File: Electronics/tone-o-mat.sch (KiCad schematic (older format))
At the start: 68 parts

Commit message: First iteration of PCB.
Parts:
- removed C?: 100uF, symbol Device:C
- removed D?: 1N4148, Diode_THT:D_DO-35_SOD27_P7.62mm_Horizontal, symbol Diode:1N4148
- removed LS?: Speaker, symbol Device:Speaker
- removed Q? (x2): BC337, Package_TO_SOT_THT:TO-92_Inline, symbol Transistor_BJT:BC337
- removed RV?: 1k, symbol Device:R_POT
- removed RV?: 4k7, symbol Device:R_POT
- removed SW?: POWER, symbol Switch:SW_DIP_x01
- removed SW?: VIBRATO, symbol Switch:SW_DIP_x01
- added C1, C3, C5, C7: 0.1uF, Capacitor_SMD:C_1206_3216Metric_Pad1.33x1.80mm_HandSolder, symbol Device:C
- added C10: 2.2uF, Capacitor_SMD:C_1206_3216Metric_Pad1.33x1.80mm_HandSolder, symbol Device:C
- added C12: 27nF, Capacitor_SMD:C_1206_3216Metric_Pad1.33x1.80mm_HandSolder, symbol Device:C
- added C9: 100uF, Capacitor_THT:CP_Radial_D5.0mm_P2.00mm, symbol Device:C
- added D1: 1N4148, Diode_THT:D_DO-35_SOD27_P7.62mm_Horizontal, symbol Diode:1N4148
- added H1, H2, H3: MountingHole_Pad, MountingHole:MountingHole_3.2mm_M3_DIN965_Pad, symbol Mechanical:MountingHole_Pad
- added J21: USB_C_Receptacle_USB2.0, Connector_USB:USB_C_Receptacle_Amphenol_12401548E4-2A, symbol Connector:USB_C_Receptacle_USB2.0
- added LS1: Speaker, Connector_PinHeader_2.54mm:PinHeader_1x02_P2.54mm_Vertical, symbol Device:Speaker
- added Q1, Q3: BC337, Package_TO_SOT_THT:TO-92_Inline, symbol Transistor_BJT:BC337
- added R10: 2.45k, Resistor_THT:R_Axial_DIN0309_L9.0mm_D3.2mm_P12.70mm_Horizontal, symbol Device:R
- added R12: 2.59k, Resistor_THT:R_Axial_DIN0309_L9.0mm_D3.2mm_P12.70mm_Horizontal, symbol Device:R
- added R14: 2.75k, Resistor_THT:R_Axial_DIN0309_L9.0mm_D3.2mm_P12.70mm_Horizontal, symbol Device:R
- added R16: 2.91k, Resistor_THT:R_Axial_DIN0309_L9.0mm_D3.2mm_P12.70mm_Horizontal, symbol Device:R
- added R18: 3.08k, Resistor_THT:R_Axial_DIN0309_L9.0mm_D3.2mm_P12.70mm_Horizontal, symbol Device:R
- added R2: 33.3k, Resistor_THT:R_Axial_DIN0309_L9.0mm_D3.2mm_P12.70mm_Horizontal, symbol Device:R
- added R20: 3.27k, Resistor_THT:R_Axial_DIN0309_L9.0mm_D3.2mm_P12.70mm_Horizontal, symbol Device:R
- added R22: 3.46k, Resistor_THT:R_Axial_DIN0309_L9.0mm_D3.2mm_P12.70mm_Horizontal, symbol Device:R
- added R24: 3.66k, Resistor_THT:R_Axial_DIN0309_L9.0mm_D3.2mm_P12.70mm_Horizontal, symbol Device:R
- added R26: 3.88k, Resistor_THT:R_Axial_DIN0309_L9.0mm_D3.2mm_P12.70mm_Horizontal, symbol Device:R
- added R28: 4.11k, Resistor_THT:R_Axial_DIN0309_L9.0mm_D3.2mm_P12.70mm_Horizontal, symbol Device:R
- added R30: 4.35k, Resistor_THT:R_Axial_DIN0309_L9.0mm_D3.2mm_P12.70mm_Horizontal, symbol Device:R
- added R32: 4.59k, Resistor_THT:R_Axial_DIN0309_L9.0mm_D3.2mm_P12.70mm_Horizontal, symbol Device:R
- added R34: 4.84k, Resistor_THT:R_Axial_DIN0309_L9.0mm_D3.2mm_P12.70mm_Horizontal, symbol Device:R
- added R36: 5.15k, Resistor_THT:R_Axial_DIN0309_L9.0mm_D3.2mm_P12.70mm_Horizontal, symbol Device:R
- added R38: 5.49k, Resistor_THT:R_Axial_DIN0309_L9.0mm_D3.2mm_P12.70mm_Horizontal, symbol Device:R
- added R4: 2.05k, Resistor_THT:R_Axial_DIN0309_L9.0mm_D3.2mm_P12.70mm_Horizontal, symbol Device:R
- added R40: 5.85k, Resistor_THT:R_Axial_DIN0309_L9.0mm_D3.2mm_P12.70mm_Horizontal, symbol Device:R
- added R41, R57, R59: 68k, Resistor_SMD:R_1206_3216Metric_Pad1.30x1.75mm_HandSolder, symbol Device:R
- added R43, R53: 4k7, Resistor_SMD:R_1206_3216Metric_Pad1.30x1.75mm_HandSolder, symbol Device:R
- added R45: 270k, Resistor_SMD:R_1206_3216Metric_Pad1.30x1.75mm_HandSolder, symbol Device:R
- added R47: 1k, Resistor_SMD:R_1206_3216Metric_Pad1.30x1.75mm_HandSolder, symbol Device:R
- added R49: 680R, Resistor_SMD:R_1206_3216Metric_Pad1.30x1.75mm_HandSolder, symbol Device:R
- added R51: 10M, Resistor_SMD:R_1206_3216Metric_Pad1.30x1.75mm_HandSolder, symbol Device:R
- added R55: 56R, Resistor_SMD:R_1206_3216Metric_Pad1.30x1.75mm_HandSolder, symbol Device:R
- added R6: 2.18k, Resistor_THT:R_Axial_DIN0309_L9.0mm_D3.2mm_P12.70mm_Horizontal, symbol Device:R
- added R61: 3k3, Resistor_SMD:R_1206_3216Metric_Pad1.30x1.75mm_HandSolder, symbol Device:R
- added R8: 2.32k, Resistor_THT:R_Axial_DIN0309_L9.0mm_D3.2mm_P12.70mm_Horizontal, symbol Device:R
- added RV1: 4k7, Potentiometer_THT:Potentiometer_Alps_RK09K_Single_Vertical, symbol Device:R_POT
- added RV2: 1k, Potentiometer_THT:Potentiometer_Alps_RK097_Single_Horizontal, symbol Device:R_POT
- added SW1: VIBRATO, Button_Switch_THT:OS102011MS2QN1, symbol Switch:SW_DIP_x01
- added SW2: POWER, Button_Switch_THT:OS102011MS2QN1, symbol Switch:SW_DIP_x01
- added U2: NE555PS, Package_SO:SOIC-8_3.9x4.9mm_P1.27mm, symbol Timer:NE555PS
- C11, C13, C2, C4, C6, C8: renamed from C?; footprint (none) -> Capacitor_THT:C_Disc_D3.0mm_W2.0mm_P2.50mm
- J1, J16, J4, J9: renamed from J?; footprint (none) -> Connector_Pin:Tone-O-Mat-Left-Pad
- J10, J12, J14, J17, J19, J2, J5, J7: renamed from J?; footprint (none) -> Connector_Pin:Tone-O-Mat-Top-Pad
- J11, J13, J18, J6: renamed from J?; footprint (none) -> Connector_Pin:Tone-O-Mat-Mid-Pad
- J15, J20, J3, J8: renamed from J?; footprint (none) -> Connector_Pin:Tone-O-Mat-Right-Pad
- R1, R11, R13, R15, R17, R19, R21, R23, R25, R27, R29, R3, R31, R33, R35, R37, R39, R5, R7, R9: renamed from R?; footprint (none) -> Resistor_SMD:R_1206_3216Metric_Pad1.30x1.75mm_HandSolder
- R42, R44, R46, R48, R50, R52, R54, R56, R58, R60, R62: renamed from R?; footprint (none) -> Resistor_THT:R_Axial_DIN0309_L9.0mm_D3.2mm_P12.70mm_Horizontal
- STYLUS1: renamed from STYLUS; footprint (none) -> Connector_Pin:Pin_D1.3mm_L11.0mm
- U1: renamed from U?; footprint (none) -> Package_DIP:DIP-8_W7.62mm_LongPads
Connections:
- net +5V: now also C9.1, J21.A4 (VBUS), J21.A9 (VBUS), J21.B4 (VBUS), J21.B9 (VBUS), Q1.1 (C), R41.2, R43.1, R47.1, U2.4 (R), U2.8 (VCC)
- net GND: now also J21.A1 (GND), J21.A12 (GND), J21.B1 (GND), J21.B12 (GND), SW2.1
- net at J1.1 (Pin_1), R1.1, R3.2: now also R2.1, R4.2
- net at R1.2, R50.1: now also R2.2, R49.1
- net at J2.1 (Pin_1), R3.1, R5.2: now also R4.1, R6.2
- net at J3.1 (Pin_1), R5.1, R7.2: now also R6.1, R8.2
- net at J4.1 (Pin_1), R7.1, R9.2: now also R10.2, R8.1
- net at J5.1 (Pin_1), R11.2, R9.1: now also R10.1, R12.2
- net at J6.1 (Pin_1), R11.1, R13.2: now also R12.1, R14.2
- net at J7.1 (Pin_1), R13.1, R15.2: now also R14.1, R16.2
- net at J8.1 (Pin_1), R15.1, R17.2: now also R16.1, R18.2
- net at J9.1 (Pin_1), R17.1, R19.2: now also R18.1, R20.2
- net at J10.1 (Pin_1), R19.1, R21.2: now also R20.1, R22.2
- net at J11.1 (Pin_1), R21.1, R23.2: now also R22.1, R24.2
- net at J12.1 (Pin_1), R23.1, R25.2: now also R24.1, R26.2
- net at J13.1 (Pin_1), R25.1, R27.2: now also R26.1, R28.2
- net at J14.1 (Pin_1), R27.1, R29.2: now also R28.1, R30.2
- net at J15.1 (Pin_1), R29.1, R31.2: now also R30.1, R32.2
- net at J16.1 (Pin_1), R31.1, R33.2: now also R32.1, R34.2
- net at J17.1 (Pin_1), R33.1, R35.2: now also R34.1, R36.2
- net at J18.1 (Pin_1), R35.1, R37.2: now also R36.1, R38.2
- net at J19.1 (Pin_1), R37.1, R39.2: now also R38.1, R40.2
- net at J20.1 (Pin_1), R39.1, R46.1: now also R40.1, R45.1
- net at C13.2, R46.2, R58.1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: now also C12.2, C9.2, LS1.2, Q3.3 (E), R45.2, R57.1, R59.1, R61.1, RV2.3, SW1.1, SW2.2, U2.1 (GND)
- net at C13.1, R50.2, U1.2 (TR)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: now also C12.1, R49.2, U2.2 (TR), U2.6 (THR)
- net at C11.1, U1.3 (Q): now also C10.1, U2.3 (Q)
- net at C2.1, R54.2, U1.5 (CV): now also C1.1, R53.2, U2.5 (CV)
- net at R44.2, U1.7 (DIS): now also D1.1 (K), Q1.2 (B), R43.2, U2.7 (DIS)
- net at R56.2: now also LS1.1, R55.2
- net at R56.1: now also R55.1, RV2.2
- net at C11.2: now also C10.2, RV2.1
- net at R48.2: now also R47.2, RV1.1
- net at R54.1: now also R53.1, RV1.2
- net at R62.2: now also R61.2, RV1.3
- net at STYLUS1.1 (Pin_1): now also D1.2 (A), Q1.3 (E)
- net at C2.2, C4.1, R42.1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: now also C1.2, C3.1, Q3.1 (C), R41.1, R51.2, SW1.2
- net at C4.2, C6.1, R58.2: now also C3.2, C5.1, R57.2
- net at C6.2, C8.1, R60.2: now also C5.2, C7.1, R59.2
- net at C8.2, R52.1: now also C7.2, Q3.2 (B), R51.1

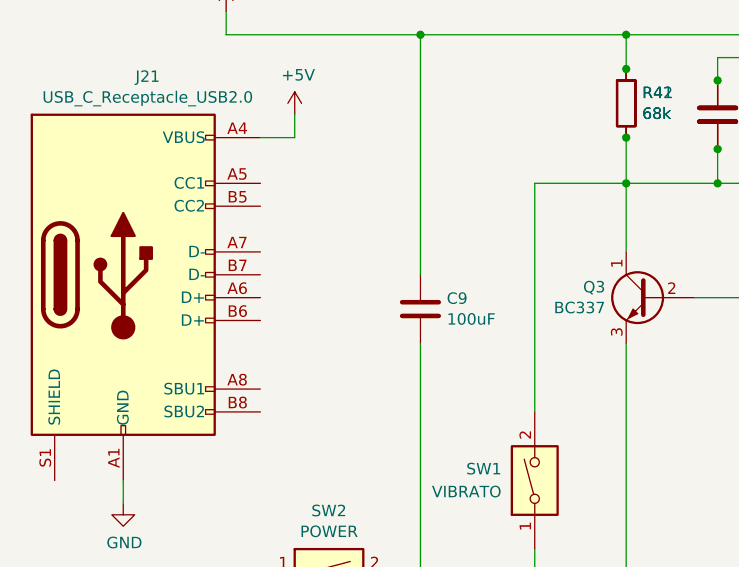
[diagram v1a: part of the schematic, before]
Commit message: Kicad 6 verze. Nové USB-C a pěknější zarovnání klávesnice. TODO: Antiparalelní schottky dioda k reproduktoru, nezapomenout na silnější trasy!
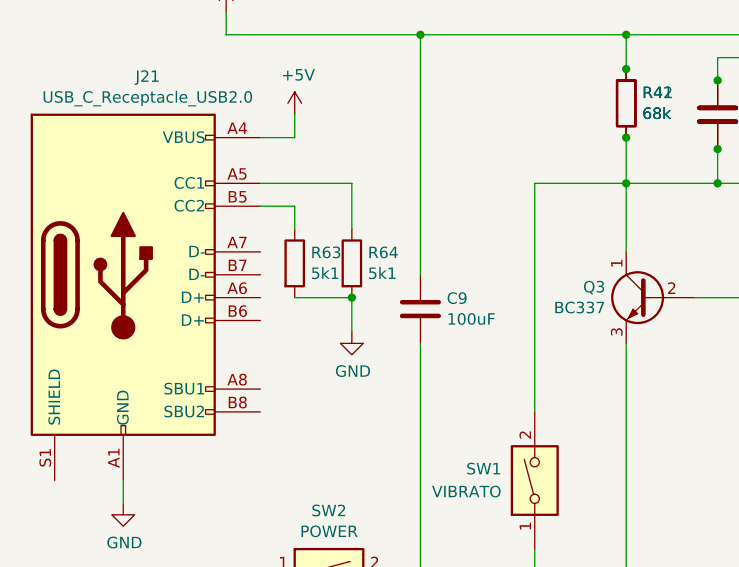
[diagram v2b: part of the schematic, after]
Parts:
- added R63, R64: 5k1, symbol Device:R
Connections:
- net GND: now also R63.2, R64.2
- net at J21.A5 (CC1): now also R64.1
- net at J21.B5 (CC2): now also R63.1
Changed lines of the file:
@@
 	1    0    0    -1
 $EndComp
+$Comp
+L power:GND #PWR0105
+U 1 1 63D7092C
+P 2200 4100
+F 0 "#PWR0105" H 2200 3850 50  0001 C CNN
+F 1 "GND" H 2205 3927 50  0000 C CNN
+F 2 "" H 2200 4100 50  0001 C CNN
+F 3 "" H 2200 4100 50  0001 C CNN
+	1    2200 4100
+	1    0    0    -1
+$EndComp
+$Comp
+L Device:R R64
+U 1 1 63D709B7
+P 2200 3800
+F 0 "R64" H 2270 3846 50  0000 L CNN
+F 1 "5k1" H 2270 3755 50  0000 L CNN
+F 2 "" V 2130 3800 50  0001 C CNN
+F 3 "~" H 2200 3800 50  0001 C CNN
+	1    2200 3800
+	1    0    0    -1
+$EndComp
+$Comp
+L Device:R R63
+U 1 1 63D714B4
+P 1950 3800
+F 0 "R63" H 2020 3846 50  0000 L CNN
+F 1 "5k1" H 2020 3755 50  0000 L CNN
+F 2 "" V 1880 3800 50  0001 C CNN
+F 3 "~" H 1950 3800 50  0001 C CNN
+	1    1950 3800
+	1    0    0    -1
+$EndComp
+Wire Wire Line
+	1800 3450 2200 3450
+Wire Wire Line
+	2200 3450 2200 3650
+Wire Wire Line
+	1950 3650 1950 3550
+Wire Wire Line
+	1950 3550 1800 3550
+Wire Wire Line
+	1950 3950 2200 3950
+Wire Wire Line
+	2200 3950 2200 4100
+Connection ~ 2200 3950
 $EndSCHEMATC
